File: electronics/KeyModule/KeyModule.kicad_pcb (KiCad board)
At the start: 2 copper layers, 20 x 100 mm, 13 parts, among them SW1 SW_Push, SW2 SW_Push, SW3 SW_Push, SW4 SW_Push, SW5 SW_Push, U1 74HC165

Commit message: Rough layout
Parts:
- J_LEFT1: footprint Connector_PinHeader_2.54mm:PinHeader_1x09_P2.54mm_Vertical -> Connector_PinHeader_2.54mm:PinHeader_1x09_P2.54mm_Vertical_SMD_Pin1Right; moved to B.Cu
- J_RIGHT1: footprint Connector_PinHeader_2.54mm:PinHeader_1x09_P2.54mm_Vertical -> Connector_PinHeader_2.54mm:PinHeader_1x09_P2.54mm_Vertical_SMD_Pin1Left; moved to B.Cu
- R1, R2, R3, R4, R5: footprint Resistor_THT:R_Axial_DIN0207_L6.3mm_D2.5mm_P7.62mm_Horizontal -> Resistor_SMD:R_0805_2012Metric; moved to B.Cu
- U1: footprint Package_DIP:DIP-16_W7.62mm -> Package_SO:SOIC-16_3.9x9.9mm_P1.27mm; moved to B.Cu
- moved SW5 83.4 mm to (77.5, 51.9)
- moved R1 65.6 mm to (69.0, 82.4), turned to -90 degrees
- moved R2 64.9 mm to (69.0, 89.4), turned to -90 degrees
- moved R3 64.3 mm to (69.0, 96.5), turned to -90 degrees
- moved SW4 56.4 mm to (77.5, 70.9)
- moved R4 54.9 mm to (86.0, 82.1), turned to -90 degrees
- moved R5 53.7 mm to (86.0, 88.5), turned to -90 degrees
- moved SW3 27.8 mm to (77.5, 89.9)
- moved SW2 26.5 mm to (77.5, 108.9)
- moved SW1 26.0 mm to (77.5, 128.0)
- moved U1 16.7 mm to (81.3, 102.0), turned to -90 degrees
- moved J_LEFT1 11.8 mm to (70.7, 127.1), turned to 180 degrees
- moved J_RIGHT1 11.7 mm to (84.3, 127.1), turned to 180 degrees

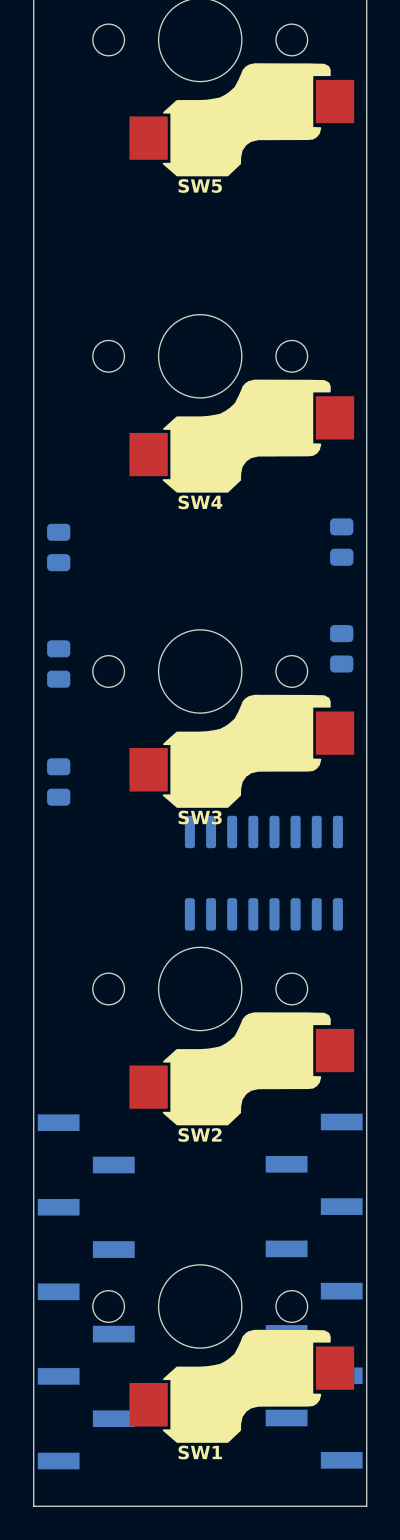
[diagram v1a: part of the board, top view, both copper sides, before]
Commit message: pcm docs, first routing attempt
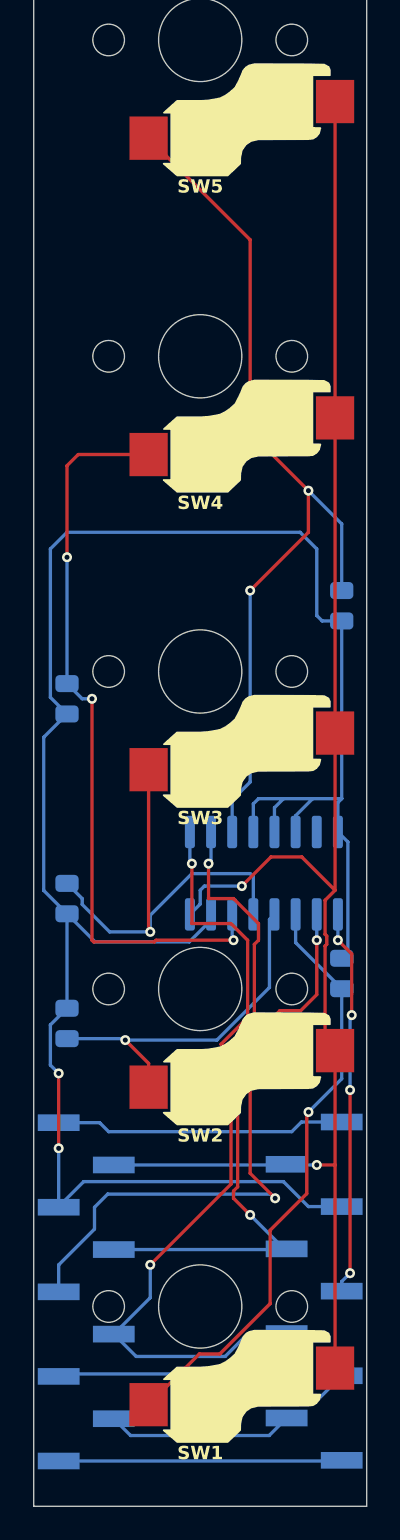
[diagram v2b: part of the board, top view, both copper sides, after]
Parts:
- moved R1 30.7 mm to (86.0, 108.0)
- moved R2 21.6 mm to (69.5, 111.0)
- moved R4 19.0 mm to (69.5, 91.5)
- moved R3 7.02 mm to (69.5, 103.5)
- moved R5 2.59 mm to (86.0, 85.9)
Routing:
- net GND: track 0.00 -> 125.3 mm, vias 0 -> 2
- net +3.3V: track 0.00 -> 101.4 mm, vias 0 -> 2
- net Net-(U1-D4): track 0.00 -> 54.4 mm, vias 0 -> 2
- net /PL: track 0.00 -> 48.3 mm, vias 0 -> 2
- net Net-(U1-D3): track 0.00 -> 44.8 mm, vias 0 -> 3
- net /CLK: track 0.00 -> 40.0 mm, vias 0 -> 2
- net /DATA_IN: track 0.00 -> 37.3 mm, vias 0 -> 2
- net Net-(U1-D0): track 0.00 -> 36.1 mm, vias 0 -> 1
- net Net-(U1-D2): track 0.00 -> 26.8 mm, vias 0 -> 1
- net /DATA_OUT: track 0.00 -> 23.2 mm, vias 0 -> 4
- net Net-(U1-D1): track 0.00 -> 21.4 mm, vias 0 -> 1
- net /LED: track 0.00 -> 18.3 mm
- net +5V: track 0.00 -> 17.5 mm
- net /SCL: track 0.00 -> 17.0 mm
- net /SDA: track 0.00 -> 11.2 mm

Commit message: wip redo the pcb design with raj
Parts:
- moved J_RIGHT1 0.69 mm to (83.7, 127.1)
- moved J_LEFT1 0.69 mm to (71.3, 127.1)
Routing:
- net /DATA_IN: track 37.3 -> 41.6 mm
- net Net-(U1-D0): track 36.1 -> 37.0 mm
- added copper zone on B.Cu, net GND
- added copper zone on F.Cu, net GND
